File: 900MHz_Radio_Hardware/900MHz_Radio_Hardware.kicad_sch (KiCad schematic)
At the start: 10 parts, among them U1 TSR_1-2450

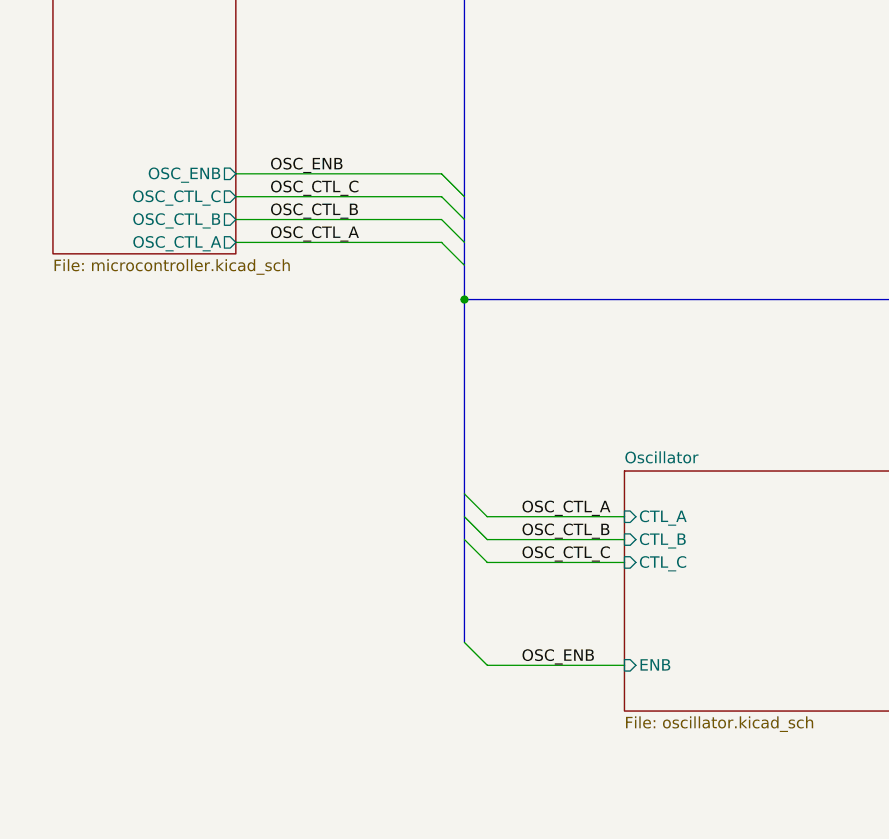
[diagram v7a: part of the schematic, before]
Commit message: Replaced oscillator Tune circuit
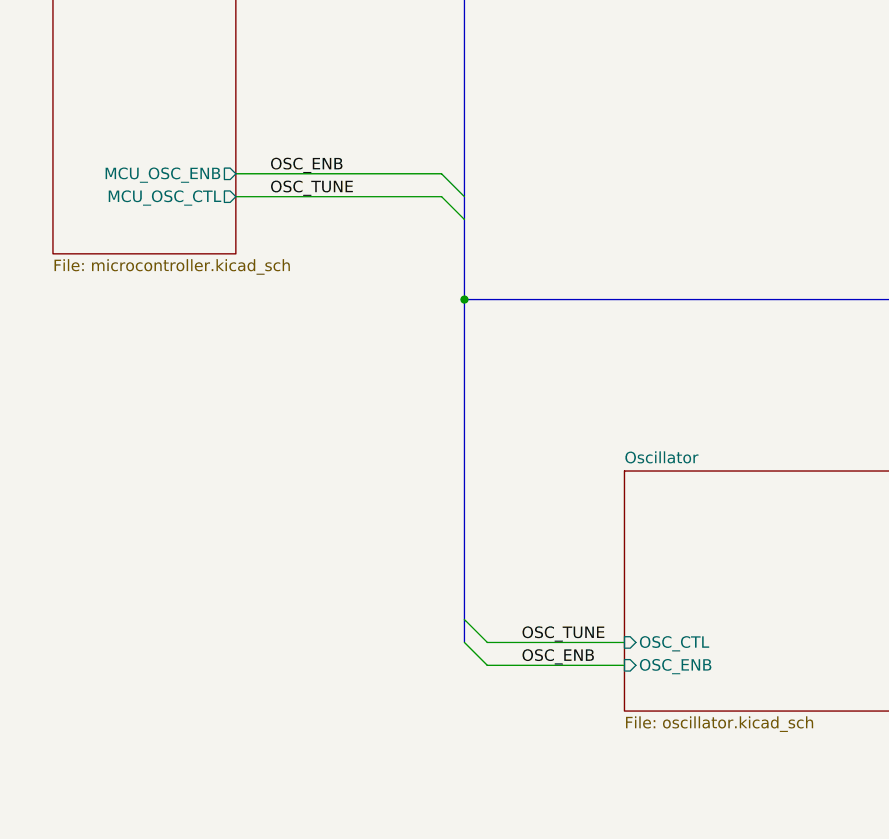
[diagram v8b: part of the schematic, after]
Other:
- sheet Microcontroller ports: added MCU_OSC_CTL, MCU_OSC_ENB; removed OSC_CTL_A, OSC_CTL_B, OSC_CTL_C, OSC_ENB
- sheet Oscillator ports: added OSC_CTL, OSC_ENB; removed CTL_A, CTL_B, CTL_C, ENB
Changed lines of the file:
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@@
   (junction (at 53.34 180.34) (diameter 0) (color 0 0 0 0)
   )
+  (bus_entry (at 60.96 120.65) (size 2.54 2.54)
+    (stroke (width 0) (type default))
+  )
   (bus_entry (at 58.42 73.66) (size 2.54 2.54)
     (stroke (width 0) (type default))
@@
     (stroke (width 0) (type default))
   )
-  (bus_entry (at 58.42 76.2) (size 2.54 2.54)
-    (stroke (width 0) (type default))
-  )
-  (bus_entry (at 60.96 109.22) (size 2.54 2.54)
-    (stroke (width 0) (type default))
-  )
-  (bus_entry (at 60.96 111.76) (size 2.54 2.54)
-    (stroke (width 0) (type default))
-  )
-  (bus_entry (at 58.42 78.74) (size 2.54 2.54)
-    (stroke (width 0) (type default))
-  )
   (bus_entry (at 60.96 123.19) (size 2.54 2.54)
     (stroke (width 0) (type default))
   )
-  (bus_entry (at 60.96 106.68) (size 2.54 2.54)
-    (stroke (width 0) (type default))
-  )
   (wire (pts (xy 26.67 167.64) (xy 30.48 167.64))
     (stroke (width 0) (type default))
@@
     (stroke (width 0) (type default))
   )
-  (wire (pts (xy 63.5 109.22) (xy 78.74 109.22))
+  (wire (pts (xy 30.48 177.8) (xy 30.48 180.34))
+    (stroke (width 0) (type default))
+  )
+  (bus (pts (xy 60.96 21.59) (xy 60.96 73.66))
+    (stroke (width 0) (type default))
+  )
+  (wire (pts (xy 90.17 165.1) (xy 90.17 167.64))
+    (stroke (width 0) (type default))
+  )
+  (wire (pts (xy 63.5 123.19) (xy 78.74 123.19))
     (stroke (width 0) (type default))
   )
@@
     (stroke (width 0) (type default))
   )
-  (wire (pts (xy 30.48 177.8) (xy 30.48 180.34))
-    (stroke (width 0) (type default))
-  )
-  (bus (pts (xy 60.96 21.59) (xy 60.96 73.66))
-    (stroke (width 0) (type default))
-  )
-  (wire (pts (xy 90.17 165.1) (xy 90.17 167.64))
-    (stroke (width 0) (type default))
-  )
-  (bus (pts (xy 60.96 81.28) (xy 60.96 85.09))
-    (stroke (width 0) (type default))
-  )
   (wire (pts (xy 107.95 185.42) (xy 107.95 187.96))
     (stroke (width 0) (type default))
@@
     (stroke (width 0) (type default))
   )
-  (wire (pts (xy 63.5 111.76) (xy 78.74 111.76))
-    (stroke (width 0) (type default))
-  )
   (wire (pts (xy 30.48 180.34) (xy 41.91 180.34))
     (stroke (width 0) (type default))
@@
     (stroke (width 0) (type default))
   )
-  (wire (pts (xy 35.56 78.74) (xy 58.42 78.74))
-    (stroke (width 0) (type default))
-  )
-  (bus (pts (xy 60.96 109.22) (xy 60.96 111.76))
-    (stroke (width 0) (type default))
-  )
-  (bus (pts (xy 60.96 78.74) (xy 60.96 81.28))
-    (stroke (width 0) (type default))
-  )
   (wire (pts (xy 30.48 167.64) (xy 41.91 167.64))
     (stroke (width 0) (type default))
@@
     (stroke (width 0) (type default))
   )
-  (wire (pts (xy 63.5 114.3) (xy 78.74 114.3))
+  (bus (pts (xy 60.96 85.09) (xy 260.35 85.09))
+    (stroke (width 0) (type default))
+  )
+  (wire (pts (xy 64.77 165.1) (xy 64.77 167.64))
+    (stroke (width 0) (type default))
+  )
+  (wire (pts (xy 63.5 125.73) (xy 78.74 125.73))
+    (stroke (width 0) (type default))
+  )
+  (wire (pts (xy 30.48 189.23) (xy 30.48 190.5))
+    (stroke (width 0) (type default))
+  )
+  (wire (pts (xy 53.34 165.1) (xy 53.34 167.64))
+    (stroke (width 0) (type default))
+  )
+  (wire (pts (xy 119.38 109.22) (xy 151.13 109.22))
+    (stroke (width 0) (type default))
+  )
+  (bus (pts (xy 60.96 85.09) (xy 60.96 120.65))
     (stroke (width 0) (type default))
   )
@@
     (stroke (width 0) (type default))
   )
-  (bus (pts (xy 60.96 85.09) (xy 260.35 85.09))
-    (stroke (width 0) (type default))
-  )
-  (bus (pts (xy 60.96 111.76) (xy 60.96 123.19))
-    (stroke (width 0) (type default))
-  )
-  (wire (pts (xy 64.77 165.1) (xy 64.77 167.64))
-    (stroke (width 0) (type default))
-  )
-  (wire (pts (xy 63.5 125.73) (xy 78.74 125.73))
-    (stroke (width 0) (type default))
-  )
-  (wire (pts (xy 30.48 189.23) (xy 30.48 190.5))
-    (stroke (width 0) (type default))
-  )
-  (wire (pts (xy 53.34 165.1) (xy 53.34 167.64))
-    (stroke (width 0) (type default))
-  )
-  (wire (pts (xy 119.38 109.22) (xy 151.13 109.22))
-    (stroke (width 0) (type default))
-  )
-  (bus (pts (xy 60.96 76.2) (xy 60.96 78.74))
-    (stroke (width 0) (type default))
-  )
-  (wire (pts (xy 35.56 76.2) (xy 58.42 76.2))
-    (stroke (width 0) (type default))
-  )
-  (bus (pts (xy 60.96 85.09) (xy 60.96 106.68))
-    (stroke (width 0) (type default))
-  )
-  (bus (pts (xy 60.96 106.68) (xy 60.96 109.22))
-    (stroke (width 0) (type default))
-  )
   (wire (pts (xy 53.34 180.34) (xy 53.34 177.8))
     (stroke (width 0) (type default))
   )
+  (bus (pts (xy 60.96 120.65) (xy 60.96 123.19))
+    (stroke (width 0) (type default))
+  )
   (wire (pts (xy 35.56 71.12) (xy 58.42 71.12))
     (stroke (width 0) (type default))
   )
+  (bus (pts (xy 60.96 76.2) (xy 60.96 85.09))
+    (stroke (width 0) (type default))
+  )
   (wire (pts (xy 41.91 180.34) (xy 53.34 180.34))
     (stroke (width 0) (type default))
@@
   (wire (pts (xy 26.67 180.34) (xy 30.48 180.34))
     (stroke (width 0) (type default))
-  )
-  (label "OSC_CTL_B" (at 39.37 76.2 0) (fields_autoplaced)
-    (effects (font (size 1.27 1.27)) (justify left bottom))
-  )
-  (label "OSC_CTL_B" (at 67.31 111.76 0) (fields_autoplaced)
-    (effects (font (size 1.27 1.27)) (justify left bottom))
   )
   (label "OSC_ENB" (at 67.31 125.73 0) (fields_autoplaced)
     (effects (font (size 1.27 1.27)) (justify left bottom))
   )
-  (label "OSC_CTL_A" (at 67.31 109.22 0) (fields_autoplaced)
-    (effects (font (size 1.27 1.27)) (justify left bottom))
-  )
-  (label "OSC_CTL_A" (at 39.37 78.74 0) (fields_autoplaced)
-    (effects (font (size 1.27 1.27)) (justify left bottom))
-  )
-  (label "OSC_CTL_C" (at 39.37 73.66 0) (fields_autoplaced)
-    (effects (font (size 1.27 1.27)) (justify left bottom))
-  )
   (label "OSC_ENB" (at 39.37 71.12 0) (fields_autoplaced)
     (effects (font (size 1.27 1.27)) (justify left bottom))
   )
-  (label "OSC_CTL_C" (at 67.31 114.3 0) (fields_autoplaced)
+  (label "OSC_TUNE" (at 39.37 73.66 0) (fields_autoplaced)
+    (effects (font (size 1.27 1.27)) (justify left bottom))
+  )
+  (label "OSC_TUNE" (at 67.31 123.19 0) (fields_autoplaced)
     (effects (font (size 1.27 1.27)) (justify left bottom))
   )
@@
       (effects (font (size 1.27 1.27)) (justify right))
     )
-    (pin "ENB" input (at 78.74 125.73 180)
-      (effects (font (size 1.27 1.27)) (justify left))
-    )
-    (pin "CTL_A" input (at 78.74 109.22 180)
-      (effects (font (size 1.27 1.27)) (justify left))
-    )
-    (pin "CTL_B" input (at 78.74 111.76 180)
-      (effects (font (size 1.27 1.27)) (justify left))
-    )
-    (pin "CTL_C" input (at 78.74 114.3 180)
+    (pin "OSC_CTL" input (at 78.74 123.19 180)
+      (effects (font (size 1.27 1.27)) (justify left))
+    )
+    (pin "OSC_ENB" input (at 78.74 125.73 180)
       (effects (font (size 1.27 1.27)) (justify left))
     )
@@
       (effects (font (size 1.27 1.27)) (justify left top))
     )
-    (pin "OSC_CTL_A" output (at 35.56 78.74 0)
-      (effects (font (size 1.27 1.27)) (justify right))
-    )
-    (pin "OSC_CTL_B" output (at 35.56 76.2 0)
-      (effects (font (size 1.27 1.27)) (justify right))
-    )
-    (pin "OSC_CTL_C" output (at 35.56 73.66 0)
-      (effects (font (size 1.27 1.27)) (justify right))
-    )
-    (pin "OSC_ENB" output (at 35.56 71.12 0)
-      (effects (font (size 1.27 1.27)) (justify right))
-    )
+    (pin "MCU_OSC_CTL" output (at 35.56 73.66 0)
+      (effects (font (size 1.27 1.27)) (justify right))
+    )
+    (pin "MCU_OSC_ENB" output (at 35.56 71.12 0)
+      (effects (font (size 1.27 1.27)) (justify right))
+    )
